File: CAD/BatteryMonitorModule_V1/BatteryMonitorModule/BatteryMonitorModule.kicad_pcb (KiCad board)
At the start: 2 copper layers, 74.6 x 74.6 mm, 76 parts, among them J1 J_FAN, J2 QT06ADP83H0000G, J3 J_NFC, J4 J_PANEL, J5 J_UART, J6 Conn_ARM_JTAG_SWD_10, J7 USB-C, J8 J_PANEL, K1 G5Q-14-DC12, Q1 AO4407A, Q2 AO4407A, Q3 AO3400A, Q4 MMBT2222A, Q5 2N7002, SW1 BOOT0, SW2 NRST, U1 STM32C071K8T6, U2 AP63203WU-7, U3 INA226AQDGSRQ1

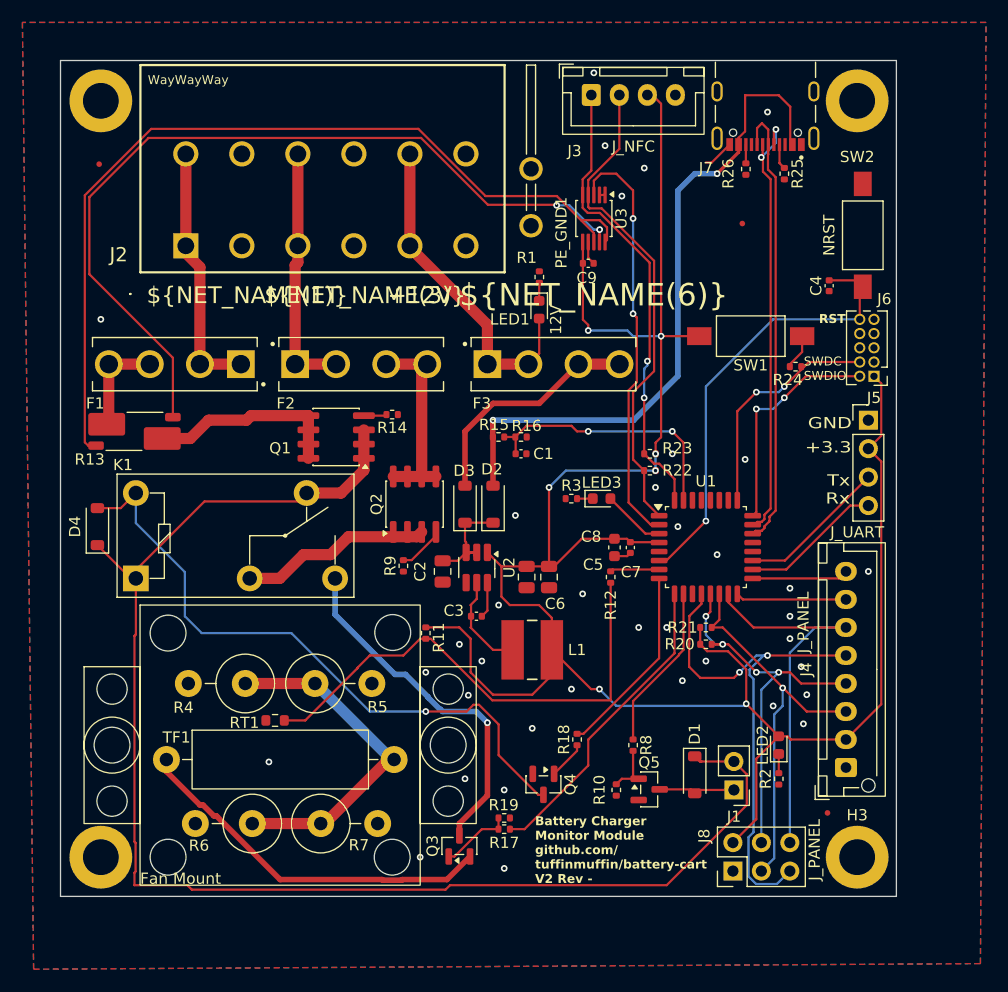
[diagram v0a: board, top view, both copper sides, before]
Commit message: found wiring error and fixed. Reved board from - to 1
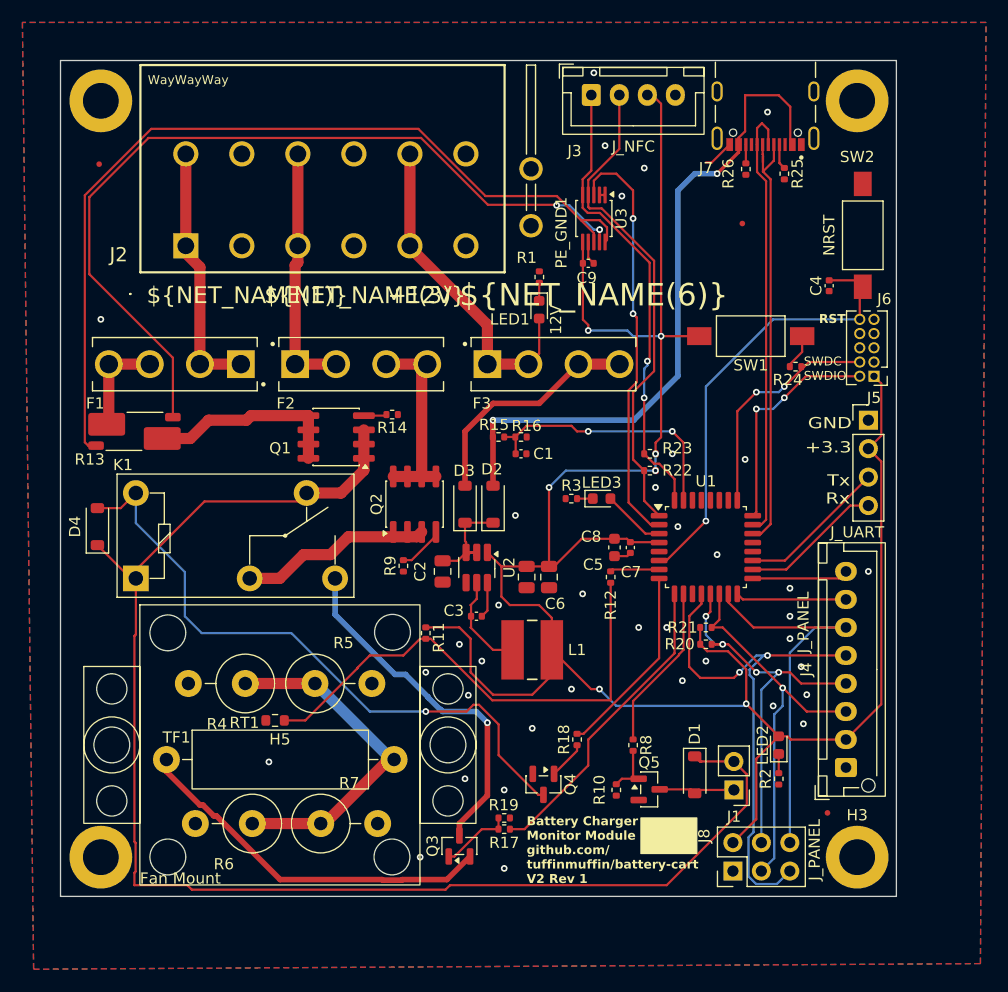
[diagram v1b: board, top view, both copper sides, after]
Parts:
- K1: value G5Q-14-DC12 -> ALQ312
- Q1, Q2: value AO4407A -> SI4435FDY-T1-GE3
- R13: value 10m -> 4m
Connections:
- U1 pad 22: USB_D+ -> USB_D-
- U1 pad 23: USB_D- -> USB_D+
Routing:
- net USB_D+: track 40.4 -> 39.4 mm
- net USB_D-: track 39.8 -> 40.0 mm, vias 2 -> 0
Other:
- board text added: "Battery Charger Monitor Module github.com/ tuffinmuffin/battery-cart V2 Rev 1"
- board text removed: "Battery Charger Monitor Module github.com/ tuffinmuffin/battery-cart V2 Rev -"
